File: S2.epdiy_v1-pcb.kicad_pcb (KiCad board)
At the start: 4 copper layers, 106.6 x 58.9 mm, 87 parts, among them J1 USB_C_Receptacle_USB2.0, J2 Jack-DC, P1 CONN_02X13, SW1 RESET, SW2 BOOT, U1 MCP1700-1202E_SOT23, U11 TP4056, U2 ESP32-S2-WROVER, U3 QFN50P700X700X100-49N, U6 ED060XC5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

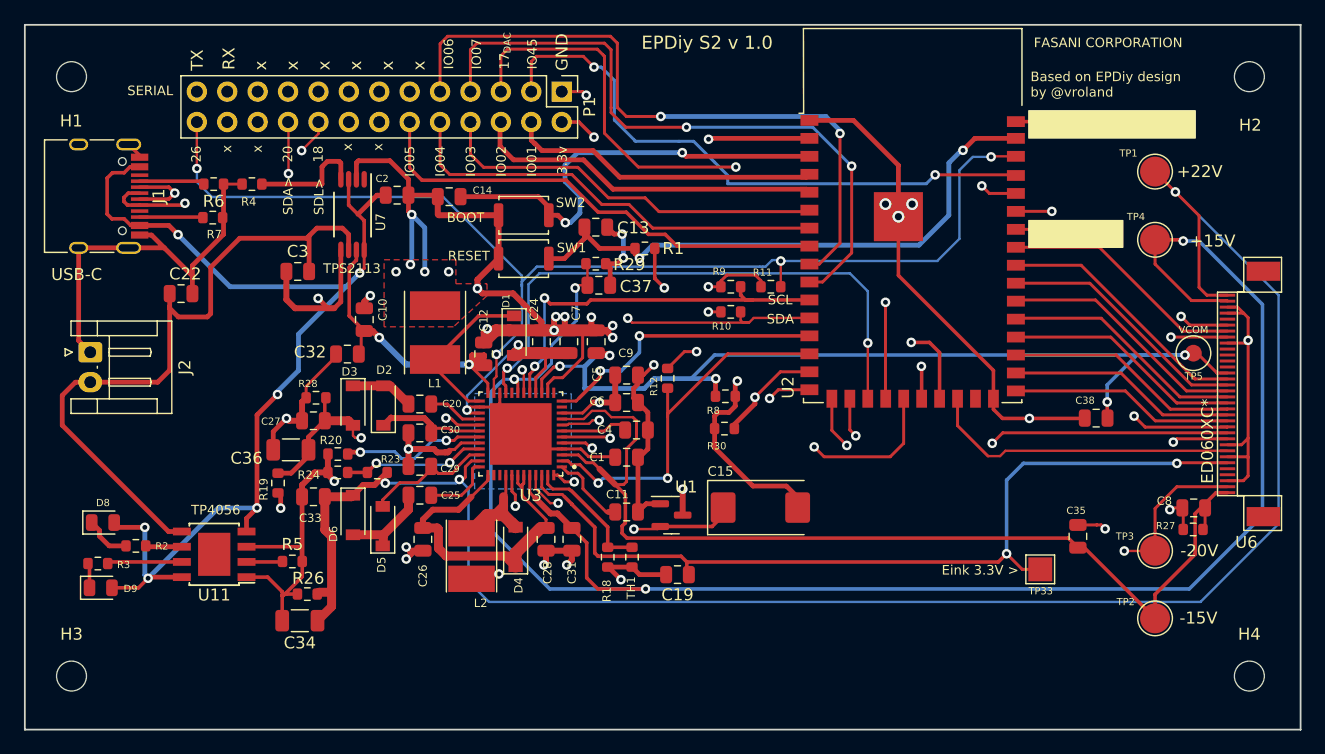
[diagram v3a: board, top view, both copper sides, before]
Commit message: Rellocate CAPs closer to EPD connector
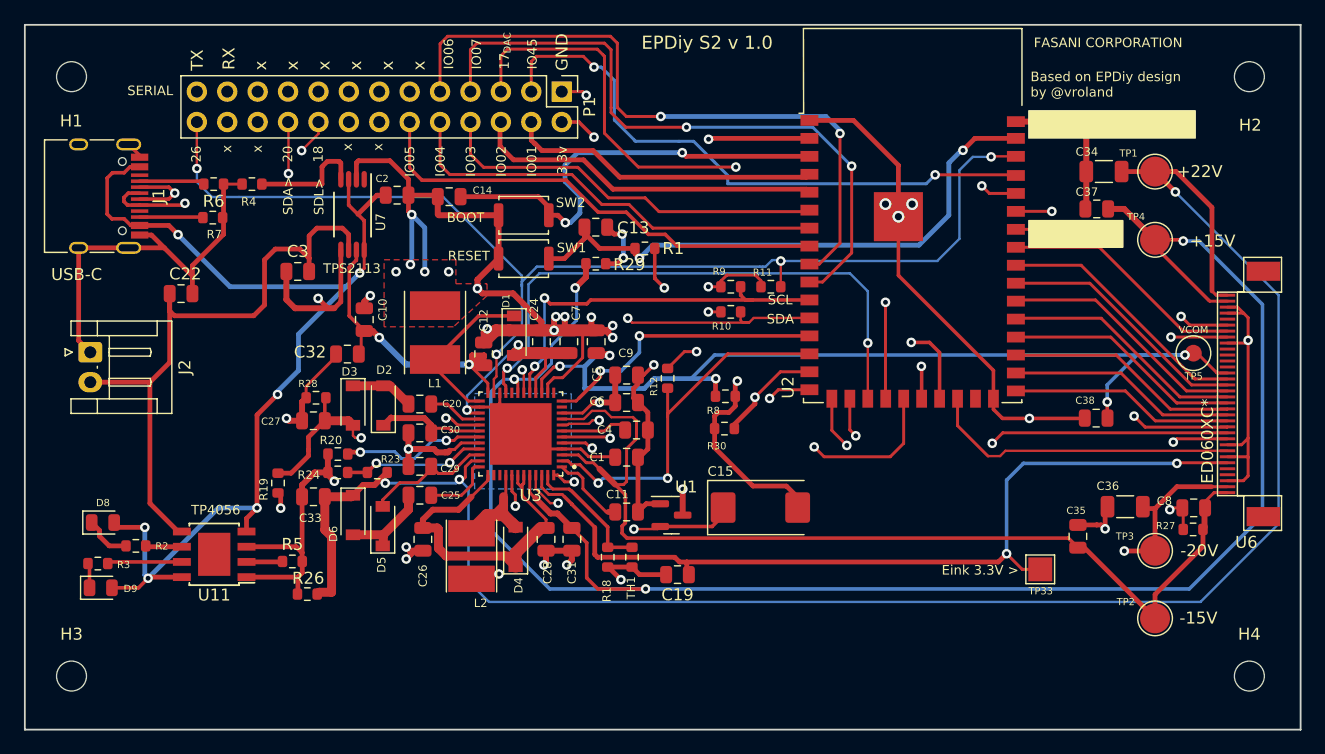
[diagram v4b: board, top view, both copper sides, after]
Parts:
- moved C34 76.9 mm to (179.2, 83.4)
- moved C36 69.9 mm to (180.9, 111.4)
- moved C37 42.1 mm to (178.6, 86.5), turned to 180 degrees
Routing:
- net BAT+: track 57.5 -> 53.0 mm
- net /15V: track 154.5 -> 158.1 mm
- net /+22V: track 154.2 -> 157.1 mm
- net GND: track 305.9 -> 308.5 mm
- net /-20V: track 108.5 -> 109.6 mm

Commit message: Update LDO caps
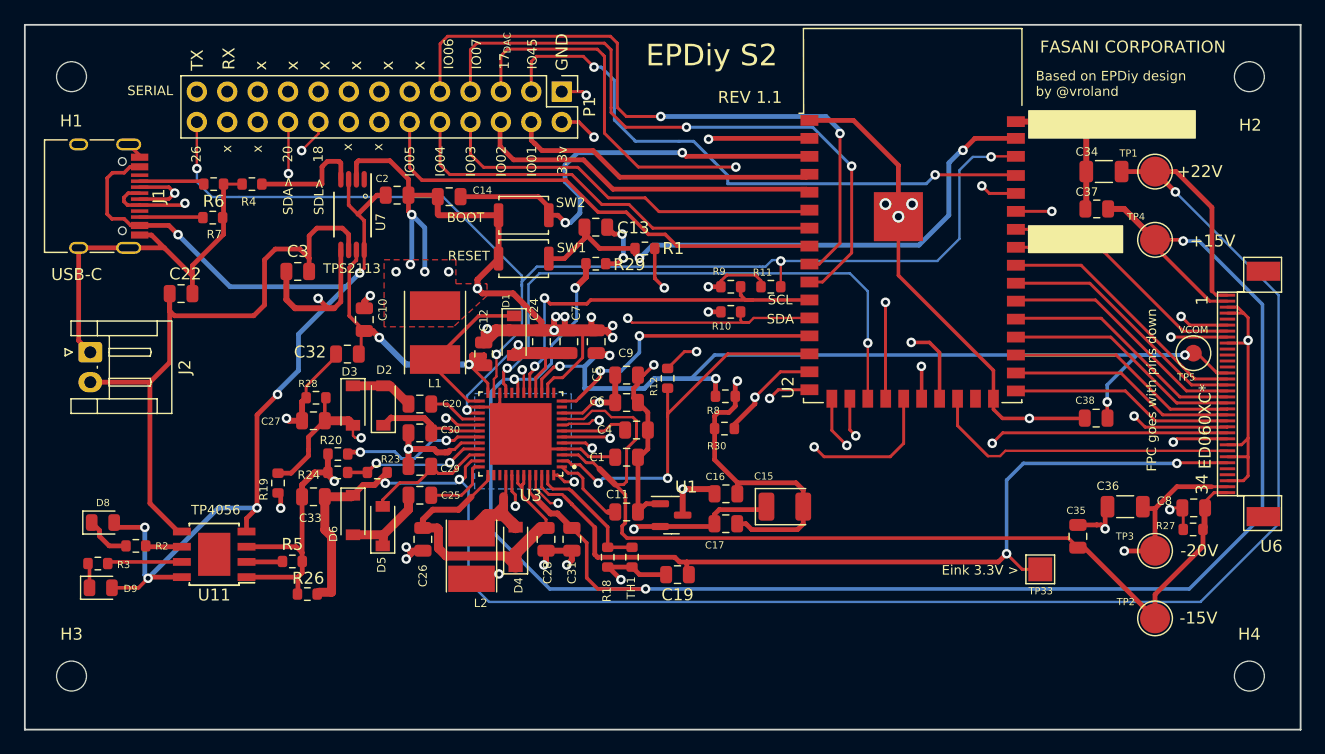
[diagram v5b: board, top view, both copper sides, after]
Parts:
- added C16: 10uF, Capacitor_SMD:C_0805_2012Metric, F.Cu at (147.6, 110.3)
- added C17: 10uF, Capacitor_SMD:C_0805_2012Metric, F.Cu at (147.6, 112.8)
- C15: value C_Polarized -> C_Polarized 100uF; footprint Capacitor_Tantalum_SMD:CP_EIA-7343-43_Kemet-X -> Capacitor_Tantalum_SMD:CP_EIA-3528-21_Kemet-B
- moved C15 2.04 mm to (152.5, 111.4)
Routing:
- net GND: track 308.5 -> 318.1 mm
- net /+3.3V: track 97.4 -> 100.6 mm
- net SW_VIN: track 86.9 -> 89.7 mm
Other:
- board text added: "1"
- board text added: "34"
- board text added: "EPDiy S2"
- board text added: "FPC goes with pins down"
- board text added: "REV 1.1"
- board text added: "°"
- board text removed: "EPDiy S2 v 1.0"

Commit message: New 1.1 design
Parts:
- added Q1: MMBT3904, Package_TO_SOT_SMD:SOT-23, F.Cu at (108.1, 96.6)
- added Q2: MMBT3904, Package_TO_SOT_SMD:SOT-23, F.Cu at (108.1, 93.2)
- added R13: 10K, Resistor_SMD:R_0603_1608Metric, F.Cu at (111.8, 96.8)
- added R14: 10K, Resistor_SMD:R_0603_1608Metric, F.Cu at (104.5, 96.6)
- U1: value MCP1700-1202E_SOT23 -> MCP1700-3302E_SOT23
- moved R1 39.4 mm to (106.5, 109.2), turned to 0 degrees
- moved C13 34.9 mm to (105.2, 103.2), turned to 180 degrees
- moved SW1 30.0 mm to (105.2, 106.5)
- moved SW2 28.6 mm to (105.2, 100.1)
- moved C14 20.0 mm to (110.8, 100.1), turned to 180 degrees
- moved C2 7.84 mm to (112.7, 88.1), turned to 0 degrees
- moved J2 1.71 mm to (92.8, 98.3)
- moved U7 0.88 mm to (116.4, 87.8)
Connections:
- net Net-(C13-Pad1) renamed ENABLE
- P1 pad 14: unconnected-(P1-Pad14) -> /SCL
- P1 pad 16: unconnected-(P1-Pad16) -> /SDA
- P1 pad 18: /SCL -> unconnected-(P1-Pad18)
- P1 pad 20: /SDA -> /DTR
- P1 pad 22: unconnected-(P1-Pad22) -> /RTS
- P1 pad 23: /RX -> unconnected-(P1-Pad23)
- P1 pad 24: unconnected-(P1-Pad24) -> /RX
- P1 pad 25: /TX -> unconnected-(P1-Pad25)
- P1 pad 26: /TPS_PWR_GOOD -> /TX
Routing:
- net BOOT_MODE: track 37.1 -> 109.5 mm
- net ENABLE: track 49.0 -> 119.8 mm
- net /-20V: track 109.6 -> 152.7 mm
- net /+3.3V: track 100.6 -> 139.6 mm
- net /TPS_PWR_GOOD: track 97.9 -> 61.7 mm, vias 4 -> 3
- net GND: track 318.1 -> 283.9 mm, vias 40 -> 46
- net /DTR: track 0.00 -> 33.3 mm, vias 0 -> 2
- net /RTS: track 0.00 -> 30.2 mm, vias 0 -> 2
- net Net-(Q2-Pad1): track 0.00 -> 6.97 mm
- net Net-(Q1-Pad1): track 0.00 -> 5.64 mm
- net /TX: track 91.1 -> 95.9 mm
- net /SCL: track 61.5 -> 57.4 mm, vias 3 -> 2
- net /SDA: track 66.1 -> 62.4 mm, vias 3 -> 2
- net /RX: track 76.2 -> 79.9 mm
- net Net-(R4-Pad1): track 9.65 -> 7.31 mm
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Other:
- board text added: "DTR"
- board text added: "RTS"
- board text added: "SDL"
- board text added: "TPS 2113"
- board text removed: "18"
- board text removed: "20"
- board text removed: "26"
- board text removed: "SDA>"
- board text removed: "SDL>"
- board text removed: "TPS2113"
